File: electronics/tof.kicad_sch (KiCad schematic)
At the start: 12 parts, among them U7 VL53L5CXV0GC/1

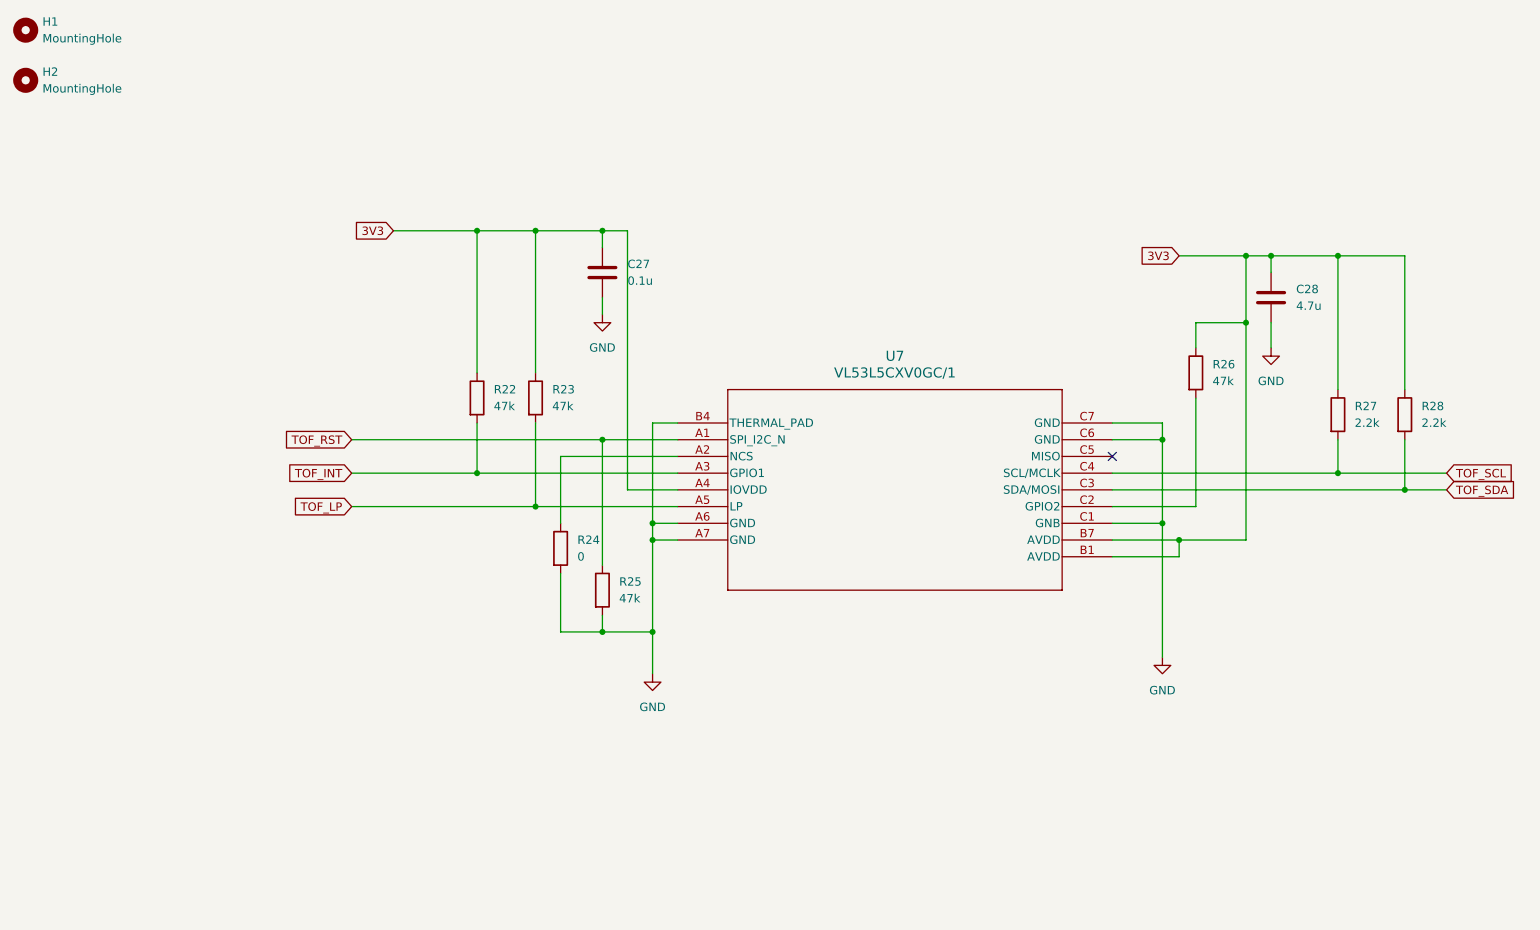
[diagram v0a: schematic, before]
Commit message: Switched to a lower cost TOF sensor.
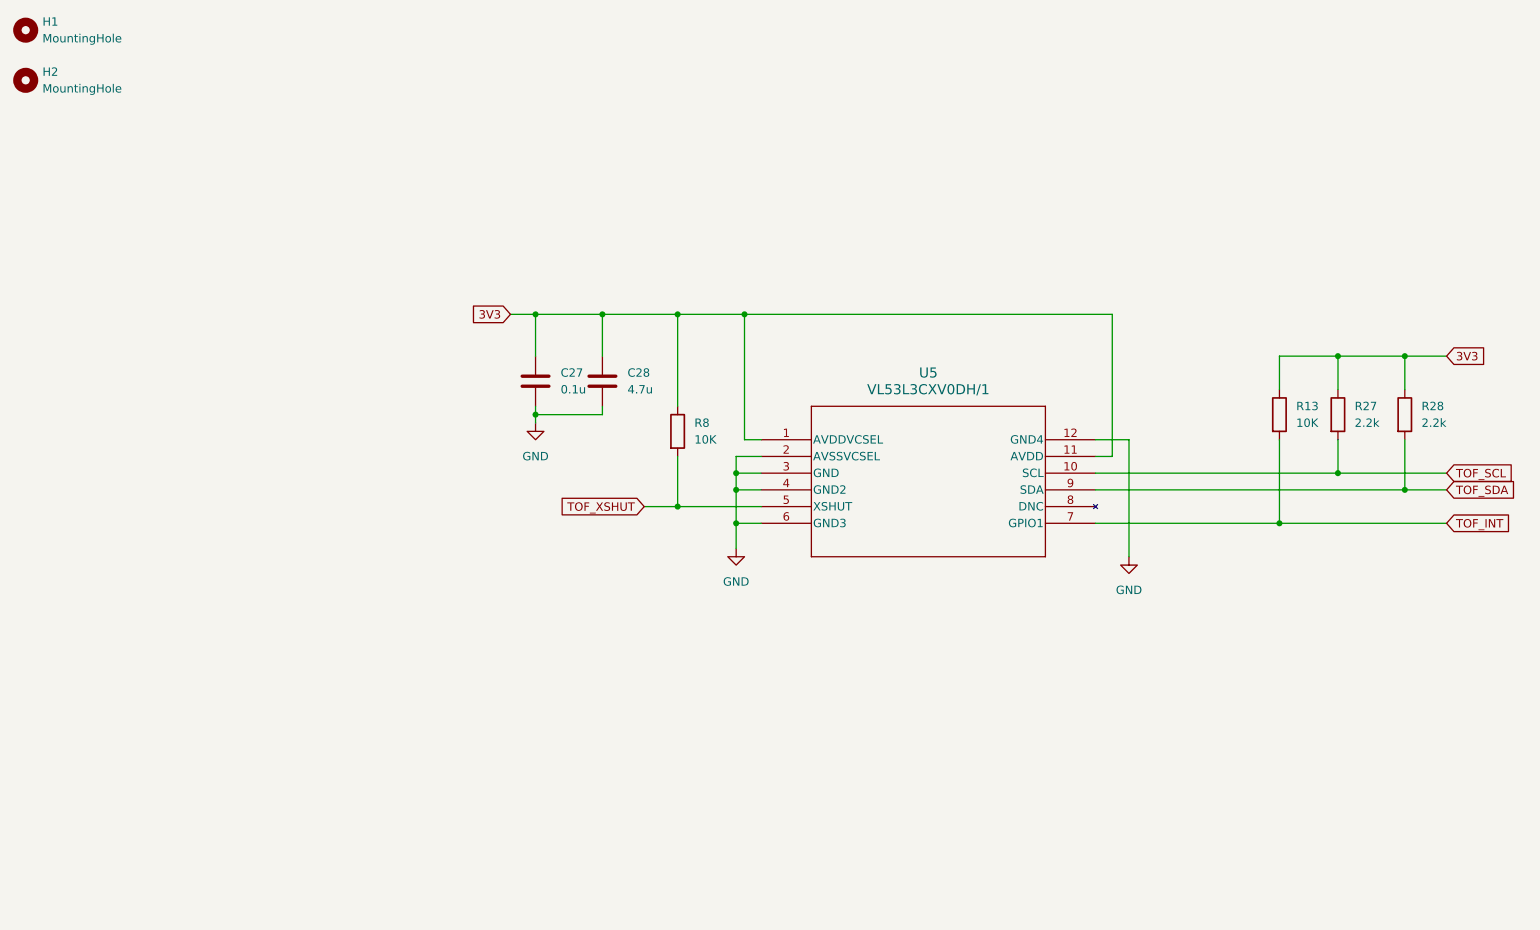
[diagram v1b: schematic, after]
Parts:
- removed R22, R23, R25, R26: 47k, Resistor_SMD:R_0402_1005Metric, symbol Device:R
- removed R24: 0, Resistor_SMD:R_0402_1005Metric, symbol Device:R
- removed U7: VL53L5CXV0GC/1, footprints:LGA_CXV0GC, symbol General:VL53L5CXV0GC_1
- added R13, R8: 10K, Resistor_SMD:R_0402_1005Metric, symbol Device:R
- added U5: VL53L3CXV0DH/1, LGA12_STM, symbol General:VL53L3CXV0DH_1
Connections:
- net 3V3: now also R13.1, R8.1, U5.1 (AVDDVCSEL), U5.11 (AVDD)
- net GND: now also U5.12 (GND4), U5.2 (AVSSVCSEL), U5.3 (GND), U5.4 (GND2), U5.6 (GND3)
- net TOF_INT: now also R13.2, U5.7 (GPIO1)
- net TOF_SCL: now also U5.10 (SCL)
- net TOF_SDA: now also U5.9 (SDA)
- new net TOF_XSHUT: R8.2, U5.5 (XSHUT)
- no-connect marks 1 -> 0
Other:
- moved on the sheet: C27, C28

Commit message: Ordered this version.
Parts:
- removed H1, H2: MountingHole, MountingHole:MountingHole_2.2mm_M2, symbol Mechanical:MountingHole
- added R22: 10K, Resistor_SMD:R_0402_1005Metric, symbol Device:R
- added U8: TCA9509DGKR, footprints:DGK8, symbol General:TCA9509DGKR
- C26: renamed from C28; footprint Capacitor_SMD:C_0805_2012Metric -> Capacitor_SMD:C_0603_1608Metric; JLCPCB (none) -> C1705
- R21: renamed from R27; JLCPCB C25744 -> C25933
- R23: renamed from R28; JLCPCB C25744 -> C25933
- U7: renamed from U5; footprint LGA12_STM -> footprints:LGA12_STM
- renumbered C27 to C25, R8 to R19, R13 to R20
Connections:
- net 3V3: now also U8.1 (VCCA); no longer C25.1, C26.1, R19.1, R20.1, R21.1, R23.1, U7.1 (AVDDVCSEL), U7.11 (AVDD)
- net GND: now also U8.4 (GND)
- net TOF_SCL: now also U8.2 (SCLA); no longer R21.2, U7.10 (SCL)
- net TOF_SDA: now also U8.3 (SDAA); no longer R23.2, U7.9 (SDA)
- new net: R22.2, U8.5 (EN)
- new net 2V8: C25.1, C26.1, R19.1, R20.1, R21.1, R22.1, R23.1, U7.1 (AVDDVCSEL), U7.11 (AVDD), U8.8 (VCCB)
- new net TOF_SCL_2V8: R21.2, U7.10 (SCL), U8.7 (SCLB)
- new net TOF_SDA_2V8: R23.2, U7.9 (SDA), U8.6 (SDAB)
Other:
- moved on the sheet: C25, C26, R19, R20, R21, R23, U7

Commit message: Refactored the design to use basic parts.
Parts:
- C26: JLCPCB C1705 -> C19666
- R21, R23: JLCPCB C25933 -> C25879
- U7: JLCPCB C1864163 -> C3178291
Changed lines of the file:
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@@
 			)
 		)
-		(property "JLCPCB" "C1705"
+		(property "JLCPCB" "C19666"
 			(at 78.74 71.12 0)
 			(effects
@@
 			)
 		)
-		(property "JLCPCB" "C1864163"
+		(property "JLCPCB" "C3178291"
 			(at 102.87 80.01 0)
 			(effects
@@
 			)
 		)
-		(property "JLCPCB" "C25933"
+		(property "JLCPCB" "C25879"
 			(at 200.66 76.2 0)
 			(effects
@@
 			)
 		)
-		(property "JLCPCB" "C25933"
+		(property "JLCPCB" "C25879"
 			(at 190.5 76.2 0)
 			(effects

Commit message: Refactoring for new IDE tools and everything.
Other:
- note added: "I2C ADDR: 0x26 (0x52 on the wire)"
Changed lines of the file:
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@@
 	(generator_version "9.0")
 	(paper "A4")
+	(text "I2C ADDR: 0x26 (0x52 on the wire)"
+		(exclude_from_sim no)
+		(at 128.27 100.33 0)
+		(effects
+			(font
+				(size 1.27 1.27)
+			)
+		)
+	)
 	(junction
 		(at 190.5 67.31)
